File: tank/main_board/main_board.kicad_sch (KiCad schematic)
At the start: 35 parts, among them J1 PowerOut, J10 PowerMotor, J11 SigOut, J12 Spk, J13 LEDs, J14 M0, J15 M1, J16 M2, J2 PowerIn, J3 Encoder0, J4 Encoder1, J5 Encoder2, J6 Encoder3, J7 Bump0, J8 Bump1, J9 Programming Header, U1 L7805, U2 ATMEGA328P-PU, U3 SN74HC595, U4 L293D, U5 L293D, Y1 Crystal

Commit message: Main Board v0.12
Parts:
- removed C2: C2, custom:C_Disc_D4.7mm_W2.5mm_P5.00mm, symbol custom:C
- removed C4: C4, custom:C_Disc_D4.7mm_W2.5mm_P5.00mm, symbol custom:C_Small
- removed D1: D, custom:D_A-405_P7.62mm_Horizontal, symbol custom:D-Device
- removed J1: PowerOut, custom:JST_EH_B2B-EH-A_1x02_P2.50mm_Vertical, symbol custom:Conn_01x02_Male
- removed J11: SigOut, custom:JST_EH_B4B-EH-A_1x04_P2.50mm_Vertical, symbol custom:Conn_01x04_Male
- removed J13: LEDs, custom:JST_EH_B4B-EH-A_1x04_P2.50mm_Vertical, symbol custom:Conn_01x04_Male
- removed J15: M1, custom:JST_EH_B2B-EH-A_1x02_P2.50mm_Vertical, symbol custom:Conn_01x02_Male
- removed J16: M2, custom:JST_EH_B2B-EH-A_1x02_P2.50mm_Vertical, symbol custom:Conn_01x02_Male
- removed J2: PowerIn, custom:JST_EH_B2B-EH-A_1x02_P2.50mm_Vertical, symbol custom:Conn_01x02_Male
- removed J5: Encoder2, custom:JST_EH_B3B-EH-A_1x03_P2.50mm_Vertical, symbol custom:Conn_01x03_Male
- removed J6: Encoder3, custom:JST_EH_B3B-EH-A_1x03_P2.50mm_Vertical, symbol custom:Conn_01x03_Male
- removed J9: Programming Header, custom:PinHeader_1x06_P2.54mm_Vertical, symbol custom:Conn_01x06_Male
- removed R1: R, custom:R_Axial_DIN0207_L6.3mm_D2.5mm_P7.62mm_Horizontal, symbol custom:R-Device
- removed R4: R10, custom:R_Axial_DIN0207_L6.3mm_D2.5mm_P7.62mm_Horizontal, symbol custom:R
- added C2: 100nF, custom:C_Disc_D4.7mm_W2.5mm_P5.00mm, symbol custom:C_Small
- added C4, C9: 100nF, custom:C_Disc_D4.7mm_W2.5mm_P5.00mm, symbol custom:C_Small-Device
- added J1: Encoder0, custom:JST_EH_B3B-EH-A_1x03_P2.50mm_Vertical, symbol custom:Conn_01x03_Male
- added J11: M0, custom:JST_EH_B2B-EH-A_1x02_P2.50mm_Vertical, symbol custom:Conn_01x02_Male
- added J13: M2, custom:JST_EH_B2B-EH-A_1x02_P2.50mm_Vertical, symbol custom:Conn_01x02_Male
- added J15: LEDs, custom:JST_EH_B4B-EH-A_1x04_P2.50mm_Vertical, symbol custom:Conn_01x04_Male
- added J16: SigOut, custom:JST_EH_B4B-EH-A_1x04_P2.50mm_Vertical, symbol custom:Conn_01x04_Male
- added J2: Encoder1, custom:JST_EH_B3B-EH-A_1x03_P2.50mm_Vertical, symbol custom:Conn_01x03_Male
- added J5: Programming Header, custom:PinHeader_1x06_P2.54mm_Vertical, symbol custom:Conn_01x06_Male
- added J6: Bump0, custom:JST_EH_B2B-EH-A_1x02_P2.50mm_Vertical, symbol custom:Conn_01x02_Male
- added J9: PowerIn, custom:JST_EH_B2B-EH-A_1x02_P2.50mm_Vertical, symbol custom:Conn_01x02_Male
- added R1: 10k, custom:R_Axial_DIN0207_L6.3mm_D2.5mm_P7.62mm_Horizontal, symbol custom:R
- C1: value CP1 -> 10uF
- C3: value CP3 -> 10uF
- C5, C8: value C_Small -> 100nF
- C6: value C6 -> 22pF
- C7: value C7 -> 22pF
- J12: value Spk -> M1
- J14: value M0 -> Spk
- J3: value Encoder0 -> Encoder2
- J4: value Encoder1 -> Encoder3
- J7: value Bump0 -> Bump1
- J8: value Bump1 -> PowerOut
- R2: value R7 -> 10k
- R3: value R6 -> 10k
- U1: footprint Custom:L7805CV -> custom:L7805CV
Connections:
- net Gm is gone; now on net GND: J10.2 (Pin_2), U4.12 (GND), U4.13 (GND), U4.4 (GND), U4.5 (GND), U5.12 (GND), U5.13 (GND), U5.4 (GND), U5.5 (GND)
- net 4.5V: now also C8.2, J8.1 (Pin_1), U3.10 (SRCLR), C2.1, C4.1, C9.2, J1.2 (Pin_2), J15.1 (Pin_1), J2.2 (Pin_2), J5.3 (Pin_3), R1.2
- net 9V: now also J9.1 (Pin_1)
- net Bump0: now also J6.2 (Pin_2); no longer J7.2 (Pin_2)
- net Bump1: now also J7.2 (Pin_2); no longer J8.2 (Pin_2)
- net Encoder0: now also J1.1 (Pin_1); no longer J3.1 (Pin_1)
- net Encoder1: now also J2.1 (Pin_1); no longer J4.1 (Pin_1)
- net Encoder2: now also J3.1 (Pin_1)
- net Encoder3: now also J4.1 (Pin_1)
- net GND: now also C8.1, J14.1 (Pin_1), J8.2 (Pin_2), C2.2, C4.2, C9.1, J1.3 (Pin_3), J2.3 (Pin_3), J5.1 (Pin_1), J6.1 (Pin_1), J9.2 (Pin_2); no longer C8.2, J12.1 (Pin_1), J8.1 (Pin_1)
- net IRRx: now also J16.4 (Pin_4)
- net IRTx: now also J16.3 (Pin_3)
- net LED0: now also J15.2 (Pin_2), J5.4 (Pin_4)
- net LED1: now also J15.3 (Pin_3), J5.5 (Pin_5)
- net LED2: now also J15.4 (Pin_4)
- net SCL: now also J16.1 (Pin_1), R1.1; no longer R2.1
- net SDA: now also R2.1, J16.2 (Pin_2); no longer R3.1
- net SPK: now also J14.2 (Pin_2); no longer J12.2 (Pin_2)
- net at C5.1, U2.1 ((PCINT14/~{RESET})PC6): now also R3.1
- net at C5.2: now also J5.6 (Pin_6)
- net at U4.11 (3Y): now also J12.2 (Pin_2)
- net at U4.14 (4Y): now also J12.1 (Pin_1)
- net at U4.3 (1Y): now also J11.2 (Pin_2); no longer J14.2 (Pin_2)
- net at U4.6 (2Y): now also J11.1 (Pin_1); no longer J14.1 (Pin_1)
- net at U5.6 (2Y): now also J13.1 (Pin_1)
- net at U5.3 (1Y): now also J13.2 (Pin_2)
- no-connect marks 12 -> 10

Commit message: FNG WIP
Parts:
- added NT1: NetTie_2, symbol Device:NetTie_2
- added R1: R, symbol Device:R
- renumbered R1 to R2, R2 to R3, R3 to R4
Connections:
- net GND: now also NT1.2; no longer C8.1, C9.1, J10.2 (Pin_2), U4.12 (GND), U4.13 (GND), U4.4 (GND), U4.5 (GND), U5.12 (GND), U5.13 (GND), U5.4 (GND), U5.5 (GND)
- net SPK: now also R1.2; no longer U2.13 ((PCINT23/AIN1)PD7)
- new net: R1.1, U2.13 ((PCINT23/AIN1)PD7)
- new net Gm: C8.1, C9.1, J10.2 (Pin_2), NT1.1, U4.12 (GND), U4.13 (GND), U4.4 (GND), U4.5 (GND), U5.12 (GND), U5.13 (GND), U5.4 (GND), U5.5 (GND)

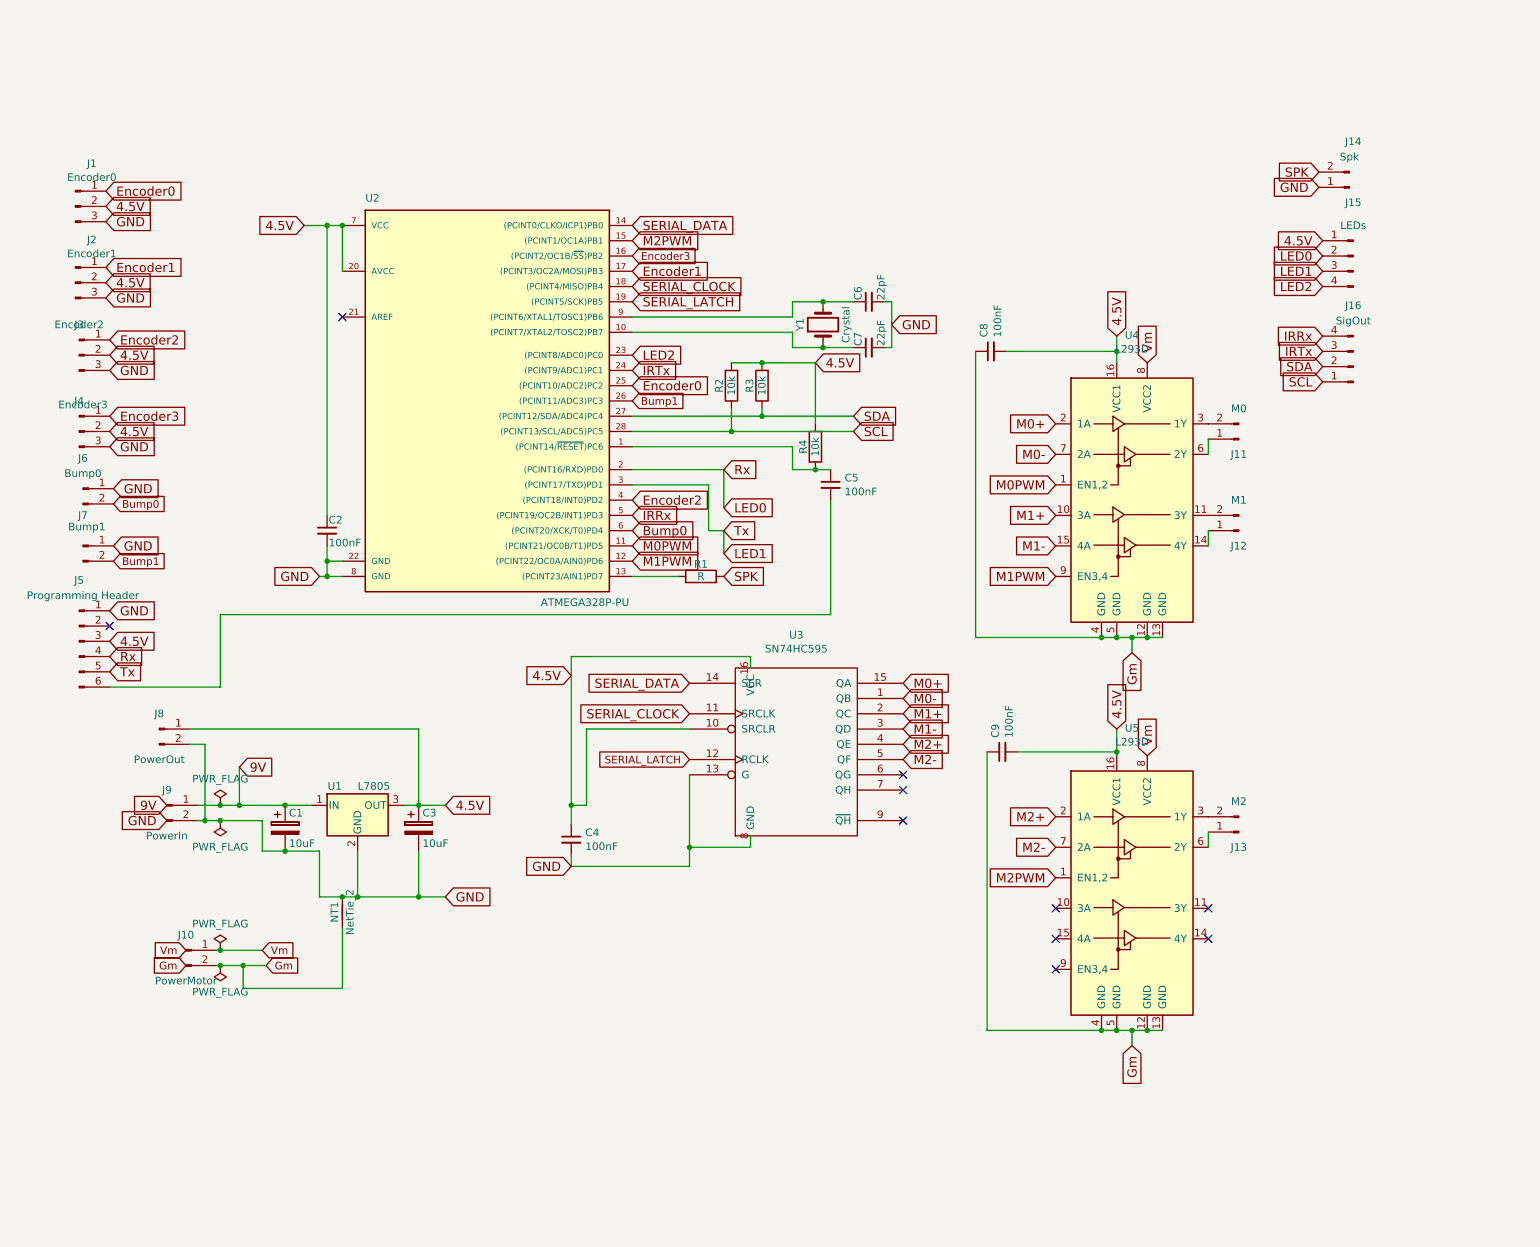
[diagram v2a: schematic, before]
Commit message: Main Board v0.15
Changes:
    - back to L293 motor driver
    - add speaker resistor
    - 3.5mm pitch screw terminals for motors and motor power
    - move programming header
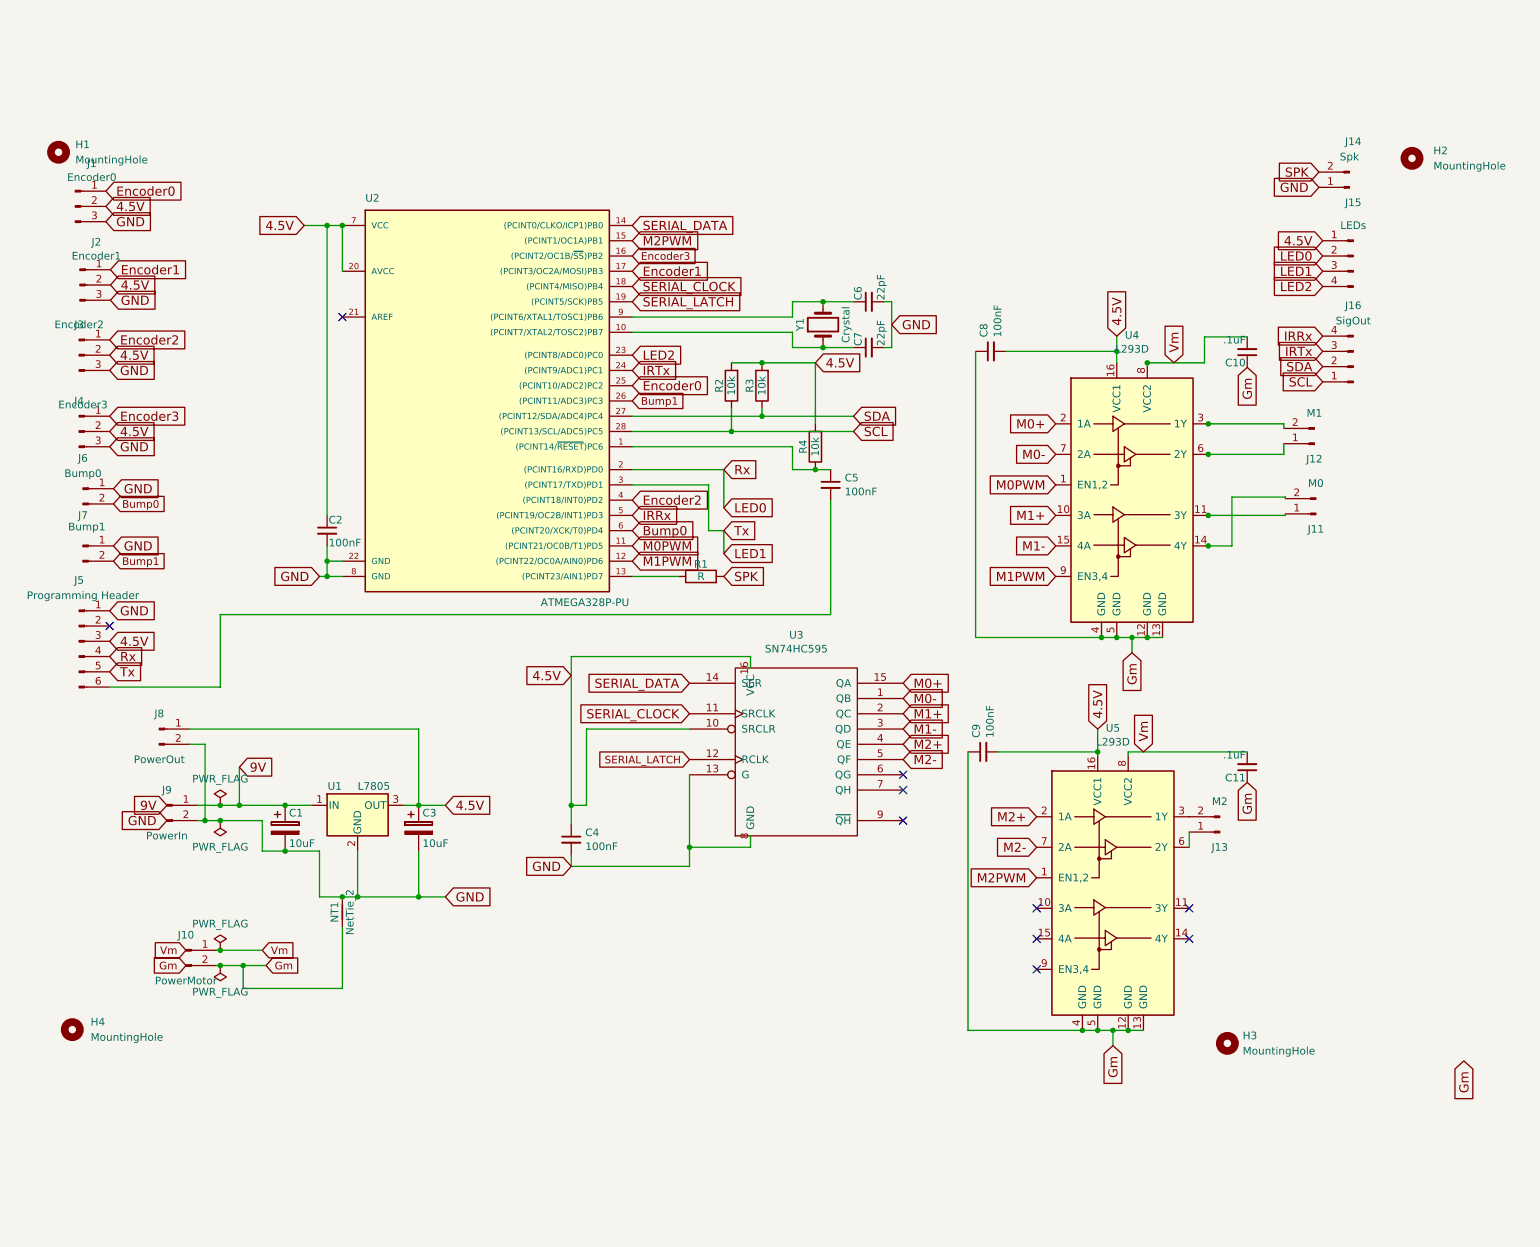
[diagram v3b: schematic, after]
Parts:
- added C10, C11: .1uF, Capacitor_THT:C_Disc_D5.0mm_W2.5mm_P2.50mm, symbol custom:C_Small
- added H1, H2, H3, H4: MountingHole, MountingHole:MountingHole_3mm, symbol Mechanical:MountingHole
- C1, C3: footprint custom:CP_Radial_D4.0mm_P2.00mm -> Capacitor_THT:CP_Radial_D4.0mm_P2.00mm
- C2, C4, C5, C6, C7, C8, C9: footprint custom:C_Disc_D4.7mm_W2.5mm_P5.00mm -> Capacitor_THT:C_Disc_D5.0mm_W2.5mm_P2.50mm
- J1, J2, J3, J4: footprint custom:JST_EH_B3B-EH-A_1x03_P2.50mm_Vertical -> Connector_JST:JST_EH_B3B-EH-A_1x03_P2.50mm_Vertical
- J10, J11, J12, J13: footprint custom:JST_EH_B2B-EH-A_1x02_P2.50mm_Vertical -> TerminalBlock_Phoenix:TerminalBlock_Phoenix_PT-1,5-2-3.5-H_1x02_P3.50mm_Horizontal
- J14, J6, J7, J8, J9: footprint custom:JST_EH_B2B-EH-A_1x02_P2.50mm_Vertical -> Connector_JST:JST_EH_B2B-EH-A_1x02_P2.50mm_Vertical
- J15, J16: footprint custom:JST_EH_B4B-EH-A_1x04_P2.50mm_Vertical -> Connector_JST:JST_EH_B4B-EH-A_1x04_P2.50mm_Vertical
- J5: footprint custom:PinHeader_1x06_P2.54mm_Vertical -> Connector_PinHeader_2.54mm:PinHeader_1x06_P2.54mm_Horizontal
- NT1: footprint (none) -> NetTie:NetTie-2_THT_Pad0.3mm
- R1: footprint (none) -> Resistor_THT:R_Axial_DIN0207_L6.3mm_D2.5mm_P7.62mm_Horizontal
- R2, R3, R4: footprint custom:R_Axial_DIN0207_L6.3mm_D2.5mm_P7.62mm_Horizontal -> Resistor_THT:R_Axial_DIN0207_L6.3mm_D2.5mm_P7.62mm_Horizontal
- U2: footprint custom:DIP-28_W7.62mm -> Package_DIP:DIP-28_W7.62mm
- U3, U4, U5: footprint custom:DIP-16_W7.62mm -> Package_DIP:DIP-16_W7.62mm
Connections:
- net Gm: now also C10.1, C11.1
- net Vm: now also C10.2, C11.2
- net at J12.1 (Pin_1): now also U4.6 (2Y); no longer U4.14 (4Y)
- net at J12.2 (Pin_2): now also U4.3 (1Y); no longer U4.11 (3Y)
- net at J11.1 (Pin_1): now also U4.11 (3Y); no longer U4.6 (2Y)
- net at J11.2 (Pin_2): now also U4.14 (4Y); no longer U4.3 (1Y)
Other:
- moved on the sheet: C9, J11, J12, J13, J2, U5

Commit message: IR Camera v0.2
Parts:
- added Q1: NPN, Package_TO_SOT_THT:TO-92, symbol Simulation_SPICE:NPN
- renumbered C9 to C8, C8 to C9, H4 to H2, H2 to H4, J14 to J11, J15 to J12, J16 to J13, J13 to J14, J12 to J15, J11 to J16, J3 to J2, J4 to J3, J5 to J4, J2 to J5, U5 to U4, U4 to U5
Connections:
- net 4.5V: now also Q1.1 (C)
- net SPK: now also R1.1, U2.13 ((PCINT23/AIN1)PD7); no longer J11.2 (Pin_2), R1.2
- new net: J11.2 (Pin_2), Q1.3 (E)
- new net: Q1.2 (B), R1.2
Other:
- moved on the sheet: C1, C10, C11, C4, C9, J1, J10, J11, J12, J13, J14, J15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

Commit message: updates for a new version of main board, mostly just KiCAD fixes but this also includes a transistor for the speaker
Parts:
- removed Q1: NPN, Package_TO_SOT_THT:TO-92, symbol Simulation_SPICE:NPN
- added Q1: 2N3904, Package_TO_SOT_THT:TO-92_Inline, symbol Transistor_BJT:2N3904
- added R5: R, Resistor_THT:R_Axial_DIN0207_L6.3mm_D2.5mm_P7.62mm_Horizontal, symbol Device:R
- C1, C3: symbol custom:CP -> Device:C_Polarized
- C10, C11, C2, C6, C7: symbol custom:C_Small -> Device:C_Small
- C4, C5: symbol custom:C_Small-Device -> Device:C_Small
- C8: renamed from C9; symbol custom:C_Small-Device -> Device:C_Small
- C9: renamed from C8; symbol custom:C_Small-Device -> Device:C_Small
- J1: symbol custom:Conn_01x03_Male -> Connector:Conn_01x03_Pin
- J10, J6, J7, J8, J9: symbol custom:Conn_01x02_Male -> Connector:Conn_01x02_Pin
- J11: renamed from J16; symbol custom:Conn_01x02_Male -> Connector:Conn_01x02_Pin
- J12: renamed from J15; symbol custom:Conn_01x02_Male -> Connector:Conn_01x02_Pin
- J13: renamed from J14; symbol custom:Conn_01x02_Male -> Connector:Conn_01x02_Pin
- J14: renamed from J11; symbol custom:Conn_01x02_Male -> Connector:Conn_01x02_Pin
- J15: renamed from J12; symbol custom:Conn_01x04_Male -> Connector:Conn_01x04_Pin
- J16: renamed from J13; symbol custom:Conn_01x04_Male -> Connector:Conn_01x04_Pin
- J2: renamed from J5; symbol custom:Conn_01x03_Male -> Connector:Conn_01x03_Pin
- J3: renamed from J2; symbol custom:Conn_01x03_Male -> Connector:Conn_01x03_Pin
- J4: renamed from J3; symbol custom:Conn_01x03_Male -> Connector:Conn_01x03_Pin
- J5: renamed from J4; symbol custom:Conn_01x06_Male -> Connector:Conn_01x06_Pin
- R2, R3, R4: symbol custom:R -> Device:R
- U1: symbol custom:L7805-Regulator_Linear -> Regulator_Linear:L7805
- U4: renamed from U5; symbol custom:L293D-Driver_Motor -> Driver_Motor:L293D
- U5: renamed from U4; symbol custom:L293D-Driver_Motor -> Driver_Motor:L293D
- Y1: symbol custom:Crystal -> Device:Crystal
- renumbered H4 to H2, H2 to H4
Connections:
- net 4.5V: now also J14.2 (Pin_2), R5.1
- net GND: now also Q1.1 (E); no longer J14.1 (Pin_1)
- net at R1.2: now also Q1.2 (B)
- new net: J14.1 (Pin_1), Q1.3 (C), R5.2
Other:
- moved on the sheet: J14, J16

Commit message: Main Board v0.16: Single power input
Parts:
- removed J10: PowerMotor, TerminalBlock_Phoenix:TerminalBlock_Phoenix_PT-1,5-2-3.5-H_1x02_P3.50mm_Horizontal, symbol Connector:Conn_01x02_Pin
- removed NT1: NetTie_2, NetTie:NetTie-2_THT_Pad0.3mm, symbol Device:NetTie_2
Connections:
- net Gm is gone; now on net GND: C10.1, C11.1, C8.1, C9.1, U4.12 (GND), U4.13 (GND), U4.4 (GND), U4.5 (GND), U5.12 (GND), U5.13 (GND), U5.4 (GND), U5.5 (GND)
- net Vm is gone; now on net 9V: C10.2, C11.2, U4.8 (VCC2), U5.8 (VCC2)

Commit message: Main Board version 0.17: - powerin is screw terminal footprint - removed PWM for turret and now both drive motors share PWM. this is because sharing the LEDs with Tx/Rx didn't work for Serial -  changed order of sigout to match sigin on turret board - removed transistor for speaker
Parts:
- removed Q1: 2N3904, Package_TO_SOT_THT:TO-92_Inline, symbol Transistor_BJT:2N3904
- removed R1, R5: R, Resistor_THT:R_Axial_DIN0207_L6.3mm_D2.5mm_P7.62mm_Horizontal, symbol Device:R
- J9: footprint Connector_JST:JST_EH_B2B-EH-A_1x02_P2.50mm_Vertical -> TerminalBlock_Phoenix:TerminalBlock_Phoenix_PT-1,5-2-3.5-H_1x02_P3.50mm_Horizontal
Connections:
- net 4.5V: now also U5.1 (EN1,2)
- net IRRx: now also J16.1 (Pin_1); no longer J16.4 (Pin_4)
- net IRTx: now also J16.2 (Pin_2); no longer J16.3 (Pin_3)
- net LED0: now also U2.15 ((PCINT1/OC1A)PB1); no longer J5.4 (Pin_4), U2.2 ((PCINT16/RXD)PD0)
- net LED1: now also U2.12 ((PCINT22/OC0A/AIN0)PD6); no longer J5.5 (Pin_5), U2.3 ((PCINT17/TXD)PD1)
- net SCL: now also J16.4 (Pin_4); no longer J16.1 (Pin_1)
- net SDA: now also J16.3 (Pin_3); no longer J16.2 (Pin_2)
- net SPK: now also J14.1 (Pin_1)
- net M0PWM renamed MPWM
- net MPWM: now also U4.9 (EN3,4)
- removed net M1PWM: U2.12 ((PCINT22/OC0A/AIN0)PD6), U4.9 (EN3,4)
- removed net M2PWM: U2.15 ((PCINT1/OC1A)PB1), U5.1 (EN1,2)
- new net Rx: J5.4 (Pin_4), U2.2 ((PCINT16/RXD)PD0)
- new net Tx: J5.5 (Pin_5), U2.3 ((PCINT17/TXD)PD1)
